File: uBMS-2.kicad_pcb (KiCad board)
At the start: 4 copper layers, 60 x 90 mm, 204 parts, among them J1 DX07S016JA1R1500, J2 XT60PW-M20, J3 XT60PW-M20, J4 Conn_01x01, J5 Conn_02x07_Odd_Even, J6 Conn_02x07_Odd_Even, J7 Conn_02x07_Odd_Even, Q1 2N7002, Q10 FQD5N20L, Q11 FQD5N20L, Q12 FQD5N20L, Q13 FQD5N20L, Q14 FQD5N20L, Q15 FQD5N20L, Q16 2N7002, Q17 2N7002, Q2 2N7002, Q3 NTD5865NL, Q4 FQD5N20L, Q5 FQD5N20L, Q6 FQD5N20L, Q7 FQD5N20L, Q8 FQD5N20L, Q9 FQD5N20L, SW1 PTS815_SJK_250_SMTR_LFS, SW2 PTS815_SJK_250_SMTR_LFS, SW3 PTS815_SJK_250_SMTR_LFS, U1 LM5166X, U10 CD74HC4067SM, U11 CD74HC4067SM, U12 CP2102N-A02-GQFN24, U2 ADS1115IDGS, U3 TLV1117-33, U4 TL431DBZ, U5 ESP32-WROOM-32, U6 TSC2012IDT, U7 MCP23017_SS, U8 MCP23008-E_P, U9 VDMG10C0

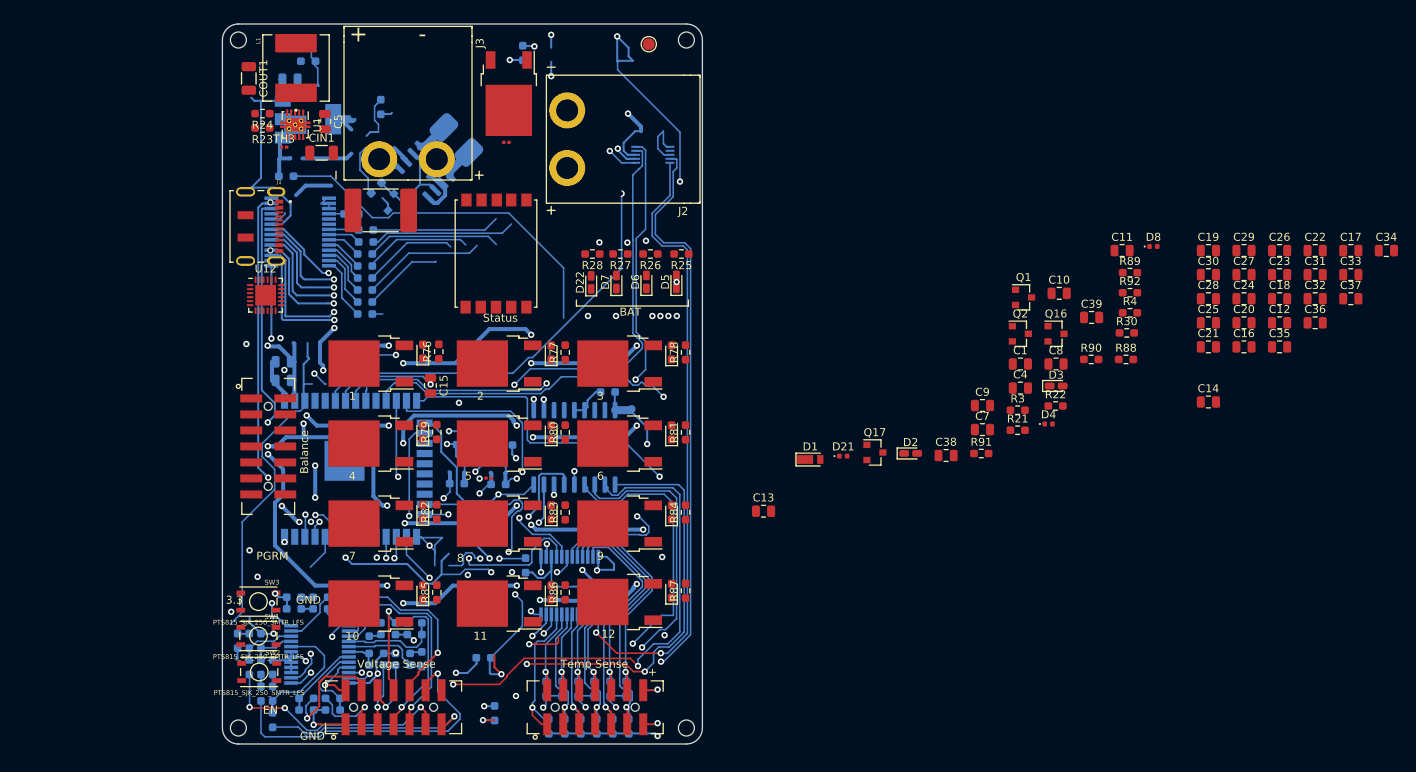
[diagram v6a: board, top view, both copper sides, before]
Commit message: Placed most components
- Make sure nets are properly connected especially with power rails from battery
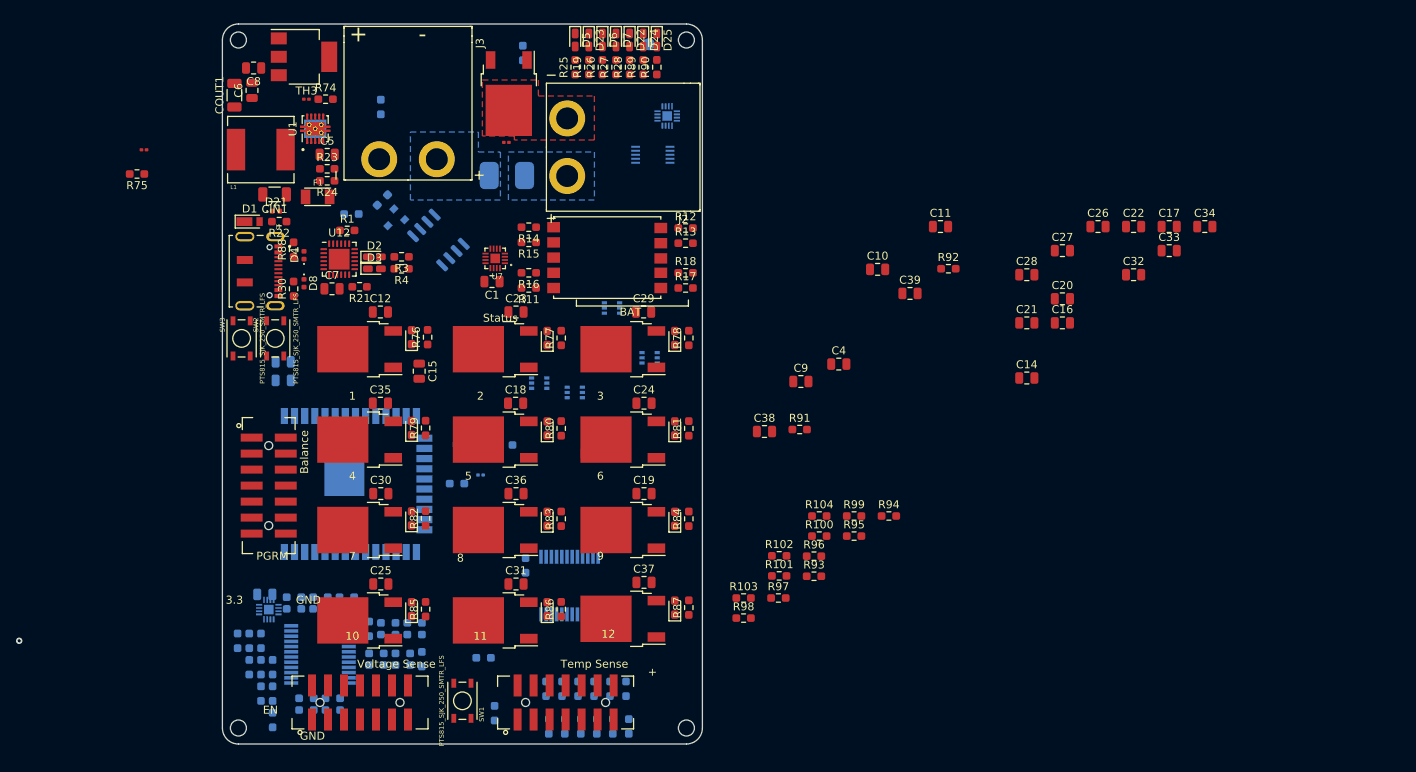
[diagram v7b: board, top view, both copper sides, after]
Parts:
- removed Q1, Q16, Q17, Q2: 2N7002, Package_TO_SOT_SMD:SOT-23
- added C40: 0.1uF, Capacitor_SMD:C_0805_2012Metric, B.Cu at (25.3, 91.3)
- added D23: YELLOW_LED, LED_SMD:LED_0603_1608Metric_Castellated, F.Cu at (65.8, 22.0)
- added D24: GREEN_LED, LED_SMD:LED_0603_1608Metric_Castellated, F.Cu at (72.6, 22.0)
- added D25: GREEN_LED, LED_SMD:LED_0603_1608Metric_Castellated, F.Cu at (74.3, 22.0)
- added R100: 10k, Resistor_SMD:R_0603_1608Metric_Pad0.98x0.95mm_HandSolder, F.Cu at (94.6, 84.0)
- added R101: 10k, Resistor_SMD:R_0603_1608Metric_Pad0.98x0.95mm_HandSolder, F.Cu at (89.6, 89.0)
- added R102: 10k, Resistor_SMD:R_0603_1608Metric_Pad0.98x0.95mm_HandSolder, F.Cu at (89.6, 86.5)
- added R103: 10k, Resistor_SMD:R_0603_1608Metric_Pad0.98x0.95mm_HandSolder, F.Cu at (85.2, 91.8)
- added R104: 10k, Resistor_SMD:R_0603_1608Metric_Pad0.98x0.95mm_HandSolder, F.Cu at (94.6, 81.5)
- added R93: 10k, Resistor_SMD:R_0603_1608Metric_Pad0.98x0.95mm_HandSolder, F.Cu at (94.0, 89.0)
- added R94: 10k, Resistor_SMD:R_0603_1608Metric_Pad0.98x0.95mm_HandSolder, F.Cu at (103.3, 81.5)
- added R95: 10k, Resistor_SMD:R_0603_1608Metric_Pad0.98x0.95mm_HandSolder, F.Cu at (99.0, 84.0)
- added R96: 10k, Resistor_SMD:R_0603_1608Metric_Pad0.98x0.95mm_HandSolder, F.Cu at (94.0, 86.5)
- added R97: 10k, Resistor_SMD:R_0603_1608Metric_Pad0.98x0.95mm_HandSolder, F.Cu at (89.5, 91.8)
- added R98: 2.2k, Resistor_SMD:R_0603_1608Metric_Pad0.98x0.95mm_HandSolder, F.Cu at (85.2, 94.3)
- added R99: 2.2k, Resistor_SMD:R_0603_1608Metric_Pad0.98x0.95mm_HandSolder, F.Cu at (99.0, 81.5)
- added U13: SN74HC595BRWNR, ClementsFootprints:QFN40P250X250X50-17N, B.Cu at (25.8, 93.2)
- added U14: SSM6N7002KFU, Package_TO_SOT_SMD:SOT-363_SC-70-6, B.Cu at (68.7, 55.5)
- added U15: SSM6N7002KFU, Package_TO_SOT_SMD:SOT-363_SC-70-6, B.Cu at (64.0, 66.1)
- added U16: SSM6N7002KFU, Package_TO_SOT_SMD:SOT-363_SC-70-6, B.Cu at (73.4, 61.7)
- added U17: SSM6N7002KFU, Package_TO_SOT_SMD:SOT-363_SC-70-6, B.Cu at (69.1, 59.2)
- added U18: SSM6N7002KFU, Package_TO_SOT_SMD:SOT-363_SC-70-6, B.Cu at (59.6, 64.9)
- C13, J4, TH2: moved to B.Cu
- C6, R11, R12, R13, R14, R15, R16, R17, R18, R74, R75, TH4, U3: moved to F.Cu
- F1: value 0ZCF0030FF2C -> 500mA PTC; footprint Fuse:Fuse_2920_7451Metric_Pad2.10x5.45mm_HandSolder -> ClementsFootprints:0ZCJ0050FF2G_3216X125N
- R1: value 2.2k -> 10k; moved to F.Cu
- R19: value 4.7k -> 470R; moved to F.Cu
- R2, R5: value 2.2k -> 47R
- R6: value 2.2k -> 10k
- R89: value 47R -> 470R
- R9: value 4.7k -> 10k
- R90: value 10k -> 470R
- R91: value 47R -> 2.2k
- R92: value 10k -> 2.2k
- U7: value MCP23017_SS -> SN74HC595BRWNR; footprint Package_SO:SSOP-28_5.3x10.2mm_P0.65mm -> ClementsFootprints:QFN40P250X250X50-17N; moved to F.Cu
- U8: value MCP23008-E_P -> SN74HC595BRWNR; footprint Package_SO:SOIC-18W_7.5x11.6mm_P1.27mm -> ClementsFootprints:QFN40P250X250X50-17N
- moved C35 112.6 mm to (39.8, 67.4)
- moved C12 112.4 mm to (39.8, 56.0)
- moved C25 108.5 mm to (39.8, 90.0)
- moved C31 107.1 mm to (56.7, 90.0)
- moved C30 107.0 mm to (39.8, 78.7)
- moved C8 106.9 mm to (23.9, 25.5), turned to 180 degrees
- moved D8 106.3 mm to (30.2, 52.4), turned to 270 degrees
- moved R88 105.0 mm to (28.9, 48.2), turned to 90 degrees
- moved R30 104.3 mm to (28.9, 53.1), turned to 90 degrees
- moved C36 102.2 mm to (56.7, 78.7)
- moved R22 99.7 mm to (27.1, 44.7), turned to 180 degrees
- moved C18 96.4 mm to (56.6, 67.4)
- moved C23 95.6 mm to (56.7, 56.0)
- moved D4 95.4 mm to (30.2, 48.9), turned to 90 degrees
- moved C37 95.2 mm to (72.7, 89.8)
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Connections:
- R1 pad 1: +3V3 -> Net-(R1-Pad1)
- R1 pad 2: /SDA_3V3 -> GND
- R19 pad 1: Net-(R19-Pad1) -> /LED_BAT_Y2
- R19 pad 2: +5V -> Net-(D23-Pad2)
- R2 pad 1: +5V -> Net-(R2-Pad1)
- R2 pad 2: /SDA_5V -> /DTR
- R26 pad 1: /LED_BAT_Y -> /LED_BAT_Y1
- R27 pad 1: /LED_BAT_G2 -> /LED_BAT_G4
- R28 pad 1: /LED_BAT_G1 -> /LED_BAT_G3
- R5 pad 1: +3V3 -> /RTS
- R5 pad 2: /SCL_3V3 -> Net-(R5-Pad2)
- R6 pad 1: +5V -> Net-(R2-Pad1)
- R6 pad 2: /SCL_5V -> GND
- R89 pad 1: Net-(Q16-Pad1) -> /LED_BAT_G2
- R89 pad 2: /DTR -> Net-(D24-Pad2)
- R9 pad 1: Net-(R9-Pad1) -> Net-(R5-Pad2)
- R9 pad 2: +5V -> GND
- R90 pad 1: Net-(Q16-Pad1) -> /LED_BAT_G1
- R90 pad 2: GND -> Net-(D25-Pad2)
- R91 pad 1: Net-(Q16-Pad2) -> +5V
- R91 pad 2: /RTS -> /SCL_5V
- R92 pad 1: Net-(Q16-Pad2) -> +5V
- R92 pad 2: GND -> /SDA_5V
- U12 pad 18: /CTS -> Net-(R1-Pad1)
- U12 pad 22: /DSR -> Net-(R1-Pad1)
- U12 pad 24: /DCD -> Net-(R1-Pad1)
- U5 pad 10: /ADC_Int -> /~OE_3V3
- U5 pad 29: /CTS -> /~SRCLR_3V3
- U5 pad 30: /DSR -> /SRCLK_3V3
- U5 pad 31: /DCD -> /SER_3V3
- U5 pad 37: Net-(U5-Pad37) -> /RCLK_3V3
- U7 pad 1: /MOD_DSC_G -> /7B
- U7 pad 10: GND -> /~SRCLR_5V
- U7 pad 11: Net-(U7-Pad11) -> /SRCLK_5V
- U7 pad 12: /SCL_5V -> /RCLK_5V
- U7 pad 13: /SDA_5V -> /~OE_5V
- U7 pad 14: Net-(U7-Pad14) -> /SREG_1_OUT
- U7 pad 15: GND -> /7A
- U7 pad 16: GND -> +5V
- U7 pad 2: Net-(U7-Pad2) -> /7C
- U7 pad 3: Net-(U7-Pad3) -> /7D
- U7 pad 4: Net-(U7-Pad4) -> /7E
- U7 pad 5: /LED_BAT_G1 -> /7F
- U7 pad 6: /LED_BAT_G2 -> /7G
- U7 pad 7: /LED_BAT_Y -> /7DP
- U7 pad 8: /LED_BAT_R -> GND
- U7 pad 9: +5V -> /SREG_2_OUT
- U8 pad 1: /SCL_5V -> /LED_BAT_G1
- U8 pad 10: /S0_V -> /~SRCLR_5V
- U8 pad 11: /S1_V -> /SRCLK_5V
- U8 pad 12: /S2_V -> /RCLK_5V
- U8 pad 13: /S3_V -> /~OE_5V
- U8 pad 14: /S0_T -> /SREG_2_OUT
- U8 pad 15: /S1_T -> /MOD_DSC_G
- U8 pad 16: /S2_T -> +5V
- U8 pad 17: /S3_T -> GND
- U8 pad 2: /SDA_5V -> /LED_BAT_G2
- U8 pad 3: GND -> /LED_BAT_G3
- U8 pad 4: GND -> /LED_BAT_G4
- U8 pad 5: Net-(R19-Pad1) -> /LED_BAT_Y1
- U8 pad 6: Net-(R19-Pad1) -> /LED_BAT_Y2
- U8 pad 7: Net-(U8-Pad7) -> /LED_BAT_R
- U8 pad 8: Net-(U8-Pad8) -> GND
- U8 pad 9: GND -> Net-(U8-Pad9)
- U9 pad 1: /7E -> Net-(R14-Pad1)
- U9 pad 10: /7G -> Net-(R12-Pad1)
- U9 pad 2: /7D -> Net-(R15-Pad1)
- U9 pad 4: /7C -> Net-(R16-Pad1)
- U9 pad 5: /7DP -> Net-(R11-Pad1)
- U9 pad 6: /7B -> Net-(R17-Pad1)
- U9 pad 7: /7A -> Net-(R18-Pad1)
- U9 pad 9: /7F -> Net-(R13-Pad1)
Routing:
- net +3V3: track 224.8 -> 60.7 mm, vias 10 -> 0
- net GND: track 163.6 -> 280.9 mm, vias 26 -> 1
- net /SCL_5V: track 94.9 -> 0.00 mm, vias 5 -> 0
- net /TempMultiplex/ESP_Temp: track 92.7 -> 0.00 mm, vias 1 -> 0
- net +5V: track 89.6 -> 0.00 mm, vias 8 -> 0
- net /SDA_5V: track 127.9 -> 40.1 mm, vias 4 -> 0
- net /TempSense: track 79.0 -> 0.00 mm, vias 2 -> 0
- net /USB_SUSPEND: track 86.6 -> 7.92 mm, vias 3 -> 0
- net /VoltageSense: track 115.1 -> 42.4 mm, vias 2 -> 0
- net /S1_V: track 74.5 -> 11.1 mm, vias 3 -> 0
- net /TempMultiplex/Power_Temp: track 80.9 -> 27.3 mm, vias 1 -> 0
- net /S0_V: track 72.3 -> 21.1 mm, vias 3 -> 0
- net Net-(U7-Pad2): track 42.3 -> 0.00 mm, vias 1 -> 0
- net /ESP_EN: track 42.2 -> 0.00 mm
- net /VoltageMultiplex/Cell11_P: track 39.8 -> 0.00 mm, vias 1 -> 0
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- added copper zone on B.Cu, net /Batt_Pos
- added copper zone on B.Cu, net /SYS_Pos
- added copper zone on F.Cu, net /SYS_RTN

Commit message: Finish PCB Layout Preliminary
- Moved around temp connections to the analogue mux to help aid layout
- Moved around voltage sense connections too
- Moved around LED status shift reg
- " and the 7 seg shift reg
- Added filled copper layers
- Removed external ADC Input
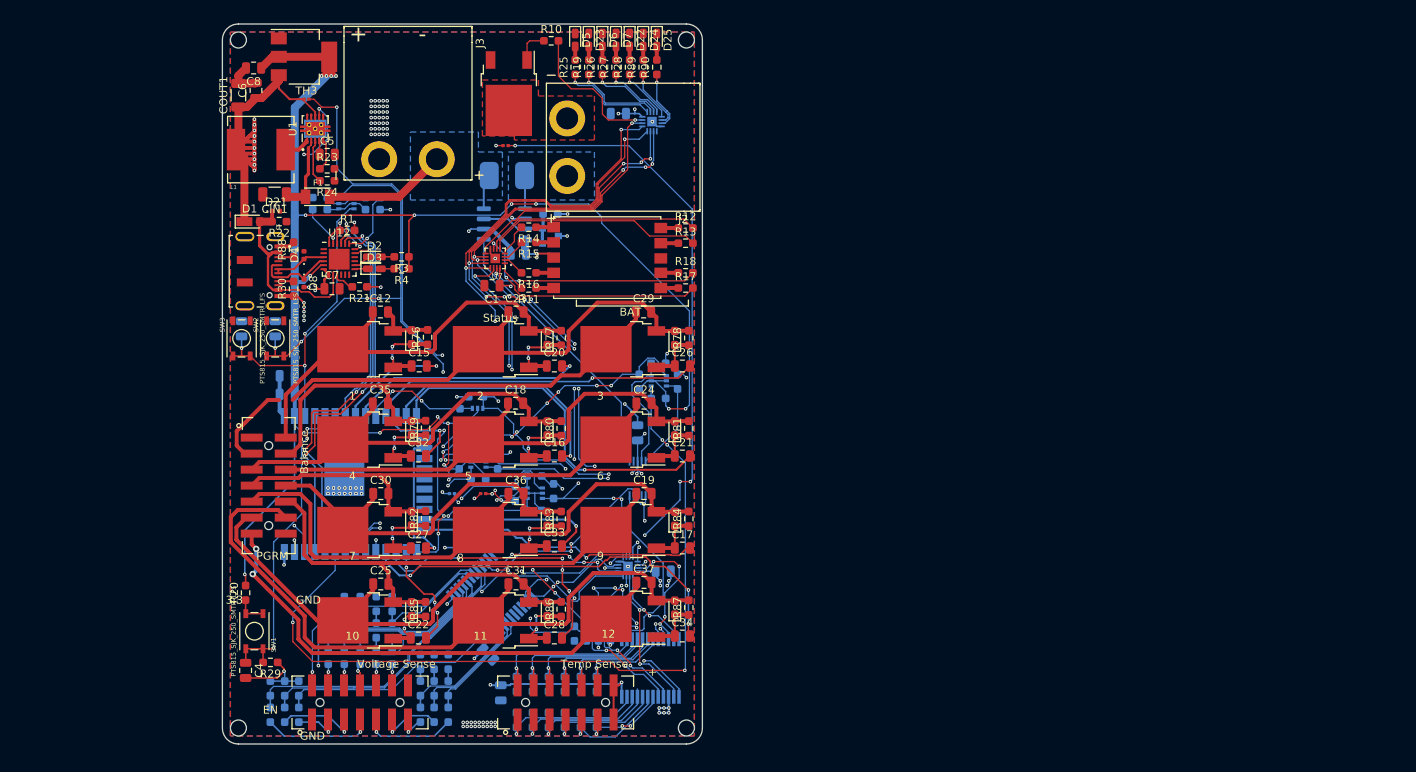
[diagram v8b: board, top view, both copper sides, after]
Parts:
- removed J4: Conn_01x01, TestPoint:TestPoint_Pad_D1.5mm
- C10, C11, C14, C38, C39, C9, R100, R101, R102, R103, R104, R74, R75, R91, R92, R93, R94, R95, R96, R97, R98, R99, TH4: moved to B.Cu
- R10, R20, R29, TH2: moved to F.Cu
- moved C22 103.1 mm to (44.5, 96.8)
- moved C32 92.2 mm to (44.5, 74.0)
- moved C27 88.7 mm to (44.5, 85.5)
- moved C33 85.3 mm to (61.5, 85.2)
- moved C39 83.7 mm to (22.4, 58.1), turned to 90 degrees
- moved C4 83.5 mm to (22.9, 100.8), turned to 270 degrees
- moved C34 83.0 mm to (77.5, 96.5)
- moved R75 80.4 mm to (65.5, 96.2), turned to 270 degrees
- moved C14 76.6 mm to (54.8, 103.6), turned to 270 degrees
- moved C28 74.5 mm to (61.5, 96.8)
- moved R74 73.7 mm to (64.0, 96.2), turned to 270 degrees
- moved C17 72.9 mm to (77.5, 85.5)
- moved R72 71.8 mm to (68.5, 96.2), turned to 270 degrees
- moved C16 65.6 mm to (61.5, 74.0)
- moved C20 64.1 mm to (61.5, 62.8)
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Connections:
- U10 pad 2: /VoltageMultiplex/Cell8_Sense -> /VoltageMultiplex/Cell3_Sense
- U10 pad 20: /VoltageMultiplex/Cell12_Sense -> /VoltageMultiplex/Cell8_Sense
- U10 pad 21: /VoltageMultiplex/Cell11_Sense -> /VoltageMultiplex/Cell10_Sense
- U10 pad 22: /VoltageMultiplex/Cell10_Sense -> /VoltageMultiplex/Cell12_Sense
- U10 pad 23: /VoltageMultiplex/Cell9_Sense -> /VoltageMultiplex/Cell2_Sense
- U10 pad 3: /VoltageMultiplex/Cell7_Sense -> /VoltageMultiplex/Cell5_Sense
- U10 pad 4: /VoltageMultiplex/Cell6_Sense -> /VoltageMultiplex/Cell7_Sense
- U10 pad 5: /VoltageMultiplex/Cell5_Sense -> /VoltageMultiplex/Cell9_Sense
- U10 pad 6: /VoltageMultiplex/Cell4_Sense -> /VoltageMultiplex/Cell11_Sense
- U10 pad 7: /VoltageMultiplex/Cell3_Sense -> /VoltageMultiplex/Cell1_P
- U10 pad 8: /VoltageMultiplex/Cell2_Sense -> /VoltageMultiplex/Cell6_Sense
- U10 pad 9: /VoltageMultiplex/Cell1_P -> /VoltageMultiplex/Cell4_Sense
- U11 pad 18: /TempMultiplex/Balance_Temp -> /TempMultiplex/CellTemp_11
- U11 pad 19: /TempMultiplex/Mosfet_Temp -> /TempMultiplex/CellTemp_9
- U11 pad 2: /TempMultiplex/CellTemp_8 -> /TempMultiplex/CellTemp_2
- U11 pad 20: /TempMultiplex/CellTemp_12 -> /TempMultiplex/CellTemp_7
- U11 pad 21: /TempMultiplex/CellTemp_11 -> /TempMultiplex/CellTemp_5
- U11 pad 22: /TempMultiplex/CellTemp_10 -> /TempMultiplex/CellTemp_3
- U11 pad 23: /TempMultiplex/CellTemp_9 -> /TempMultiplex/CellTemp_1
- U11 pad 3: /TempMultiplex/CellTemp_7 -> /TempMultiplex/CellTemp_4
- U11 pad 5: /TempMultiplex/CellTemp_5 -> /TempMultiplex/CellTemp_8
- U11 pad 6: /TempMultiplex/CellTemp_4 -> /TempMultiplex/CellTemp_10
- U11 pad 7: /TempMultiplex/CellTemp_3 -> /TempMultiplex/CellTemp_12
- U11 pad 8: /TempMultiplex/CellTemp_2 -> /TempMultiplex/Balance_Temp
- U11 pad 9: /TempMultiplex/CellTemp_1 -> /TempMultiplex/Mosfet_Temp
- U2 pad 7: /ExtADCInput -> Net-(U2-Pad7)
- U7 pad 1: /7B -> /7DP
- U7 pad 7: /7DP -> /7B
- U8 pad 1: /LED_BAT_G1 -> /LED_BAT_R
- U8 pad 2: /LED_BAT_G2 -> /LED_BAT_Y2
- U8 pad 3: /LED_BAT_G3 -> /LED_BAT_Y1
- U8 pad 5: /LED_BAT_Y1 -> /LED_BAT_G3
- U8 pad 6: /LED_BAT_Y2 -> /LED_BAT_G2
- U8 pad 7: /LED_BAT_R -> /LED_BAT_G1
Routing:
- net GND: track 280.9 -> 81.9 mm, vias 1 -> 99
- net +3V3: track 60.7 -> 241.1 mm, vias 0 -> 19
- net +5V: track 0.00 -> 145.4 mm, vias 0 -> 35
- net /RCLK_5V: track 0.00 -> 101.4 mm, vias 0 -> 10
- net /~SRCLR_5V: track 0.00 -> 99.0 mm, vias 0 -> 7
- net /~OE_5V: track 0.00 -> 93.1 mm, vias 0 -> 6
- net /SRCLK_5V: track 0.00 -> 89.7 mm, vias 0 -> 12
- net /BatteryBalance/Cell11_P: track 0.00 -> 89.5 mm
- net /SDA_3V3: track 21.6 -> 101.2 mm, vias 0 -> 4
- net /TempMultiplex/Power_Temp: track 27.3 -> 105.2 mm, vias 0 -> 5
- net /BatteryBalance/Cell2_P: track 0.00 -> 76.0 mm
- net /BatteryBalance/Cell8_P: track 0.00 -> 75.9 mm
- net /BatteryBalance/Cell5_P: track 0.00 -> 65.4 mm
- net /BatteryBalance/Cell3_P: track 0.00 -> 64.1 mm
- net /BatteryBalance/Cell9_P: track 0.00 -> 63.8 mm
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- added copper zone on In2.Cu, net +5V
- added copper zone on B.Cu, net GND
- added copper zone on F.Cu, net GND
- added copper zone on In1.Cu, net GND
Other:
- net class JLC_Outer_4_6 added: clearance 0.09, trace_width 0.09, via_dia 0.8, via_drill 0.4
- rule via_min_drill: 0.3 -> 0.2
- rule via_min_size: 0.4 -> 0.45
